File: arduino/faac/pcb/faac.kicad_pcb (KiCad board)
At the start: 2 copper layers, 5 parts, among them J1 BatCon, U1 HPD8407-F, U2 ProMini, U3 Reg3V3

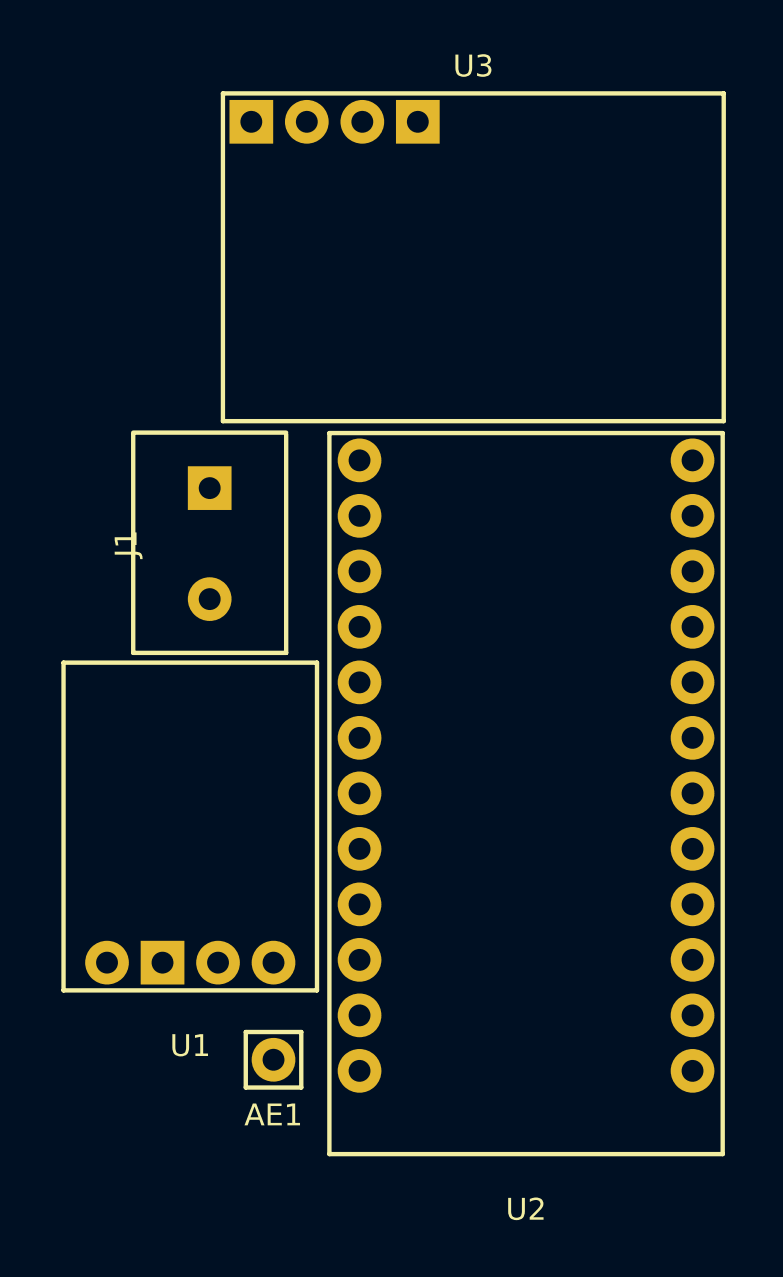
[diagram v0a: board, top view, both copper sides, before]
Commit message: faac: Add more routes
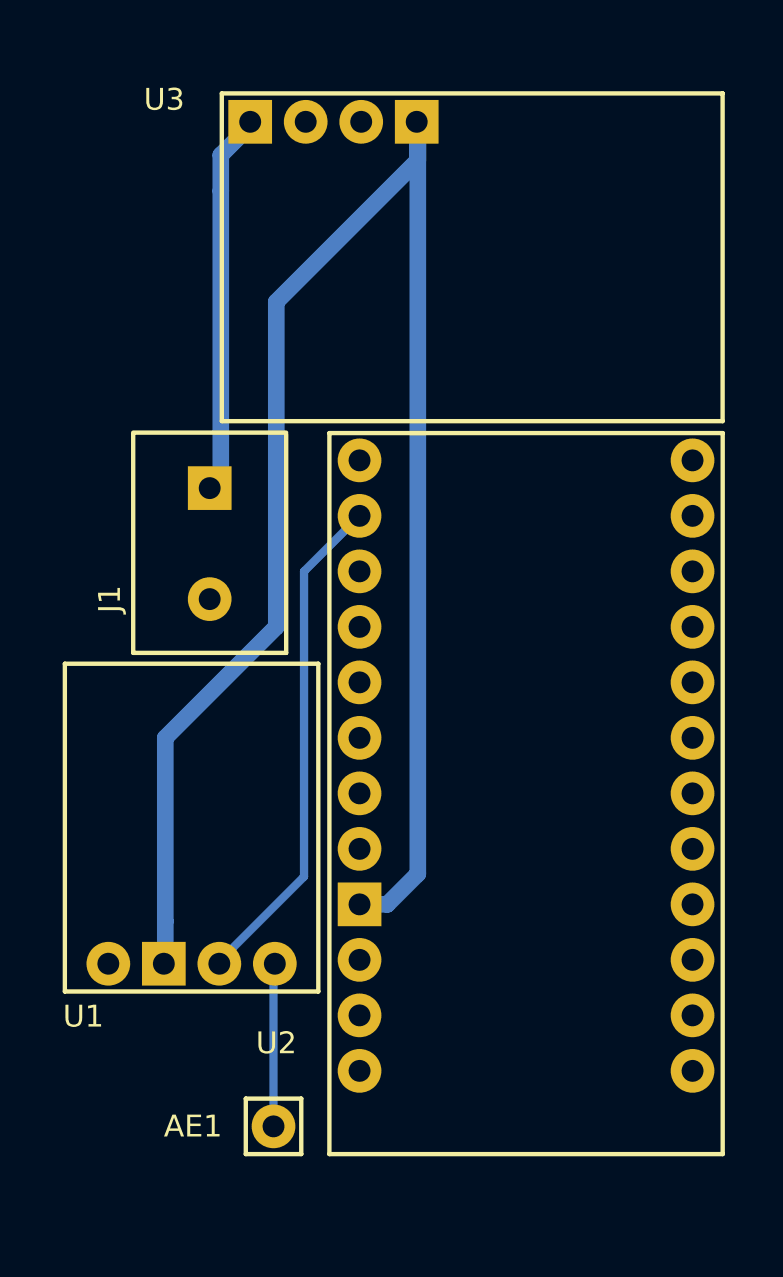
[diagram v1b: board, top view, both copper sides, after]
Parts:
- AE1: value Device_Antenna -> ANT
- moved AE1 3.05 mm to (115.4, 127.0)
- moved U1 0.08 mm to (111.7, 120.8)
- moved U3 0.05 mm to (124.5, 81.0)
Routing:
- net Net-(U1-Pad2): track 0.00 -> 80.8 mm
- net Net-(U1-Pad3): track 0.00 -> 23.0 mm
- net Net-(J1-Pad1): track 0.00 -> 17.0 mm
- net Net-(AE1-Pad1): track 0.00 -> 7.49 mm
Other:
- net class Default: clearance 0.2 -> 0.25
- rule pad_to_mask_clearance: 0.051 -> 0
- rule trace_clearance: 0.2 -> 0.25
- rule trace_min: 0.2 -> 0.25
- rule via_min_drill: 0.3 -> 0.4
- rule via_min_size: 0.4 -> 0.8
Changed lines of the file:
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@@
     (thickness 1.6)
     (drawings 0)
-    (tracks 0)
+    (tracks 16)
     (zones 0)
     (modules 5)
@@
   )
   (setup
-    (last_trace_width 0.25)
-    (trace_clearance 0.2)
+    (last_trace_width 0.381)
+    (user_trace_width 0.381)
+    (user_trace_width 0.762)
+    (trace_clearance 0.25)
     (zone_clearance 0.508)
     (zone_45_only no)
-    (trace_min 0.2)
+    (trace_min 0.25)
     (segment_width 0.2)
     (edge_width 0.15)
     (via_size 0.8)
     (via_drill 0.4)
-    (via_min_size 0.4)
-    (via_min_drill 0.3)
+    (via_min_size 0.8)
+    (via_min_drill 0.4)
     (uvia_size 0.3)
     (uvia_drill 0.1)
@@
     (pad_size 1.524 1.524)
     (pad_drill 0.762)
-    (pad_to_mask_clearance 0.051)
+    (pad_to_mask_clearance 0)
     (solder_mask_min_width 0.25)
     (aux_axis_origin 0 0)
-    (visible_elements FFFFFF7F)
+    (visible_elements 7FFFFFFF)
     (pcbplotparams
       (layerselection 0x010fc_ffffffff)
@@
   (net 25 "Net-(U2-Pad24)")
   (net_class Default "This is the default net class."
-    (clearance 0.2)
+    (clearance 0.25)
     (trace_width 0.25)
     (via_dia 0.8)
@@
     (uvia_dia 0.3)
     (uvia_drill 0.1)
+    (diff_pair_gap 0.25)
+    (diff_pair_width 0.25)
     (add_net GND)
     (add_net "Net-(AE1-Pad1)")
@@
   )
   (module myfoots:antenna (layer F.Cu)
-    (at 115.443 123.952)
-    (fp_text reference AE1 (at 0 2.54) (layer F.SilkS)
+    (at 115.443 127)
+    (fp_text reference AE1 (at -3.683 0) (layer F.SilkS)
       (effects (font (size 1 1) (thickness 0.15)))
     )
-    (fp_text value Device_Antenna (at 0 -2.54) (layer F.Fab)
+    (fp_text value ANT (at 0.127 5.08) (layer F.Fab)
       (effects (font (size 1 1) (thickness 0.15)))
     )
+    (fp_line (start -1.27 1.27) (end -1.27 -1.27) (layer F.SilkS) (width 0.2))
+    (fp_line (start 1.27 1.27) (end -1.27 1.27) (layer F.SilkS) (width 0.2))
+    (fp_line (start 1.27 -1.27) (end 1.27 1.27) (layer F.SilkS) (width 0.2))
     (fp_line (start -1.27 -1.27) (end 1.27 -1.27) (layer F.SilkS) (width 0.2))
-    (fp_line (start 1.27 -1.27) (end 1.27 1.27) (layer F.SilkS) (width 0.2))
-    (fp_line (start 1.27 1.27) (end -1.27 1.27) (layer F.SilkS) (width 0.2))
-    (fp_line (start -1.27 1.27) (end -1.27 -1.27) (layer F.SilkS) (width 0.2))
     (pad 1 thru_hole circle (at 0 0) (size 2 2) (drill 1) (layers *.Cu *.Mask)
       (net 1 "Net-(AE1-Pad1)"))
@@
   (module myfoots:BatCon (layer F.Cu)
     (at 112.522 100.33 270)
-    (fp_text reference J1 (at 0 3.81 270) (layer F.SilkS)
-      (effects (font (size 1 1) (thickness 0.2)))
-    )
-    (fp_text value BatCon (at -1.397 19.939 270) (layer F.Fab)
-      (effects (font (size 1 1) (thickness 0.2)))
-    )
+    (fp_text reference J1 (at 2.54 4.572 270) (layer F.SilkS)
+      (effects (font (size 1 1) (thickness 0.2)))
+    )
+    (fp_text value BatCon (at 0 10.922 270) (layer F.Fab)
+      (effects (font (size 1 1) (thickness 0.2)))
+    )
+    (fp_line (start -5 -3.5) (end 5 -3.5) (layer F.SilkS) (width 0.2))
+    (fp_line (start -5.08 -3.5) (end -5.08 3.5) (layer F.SilkS) (width 0.2))
+    (fp_line (start 5 -3.5) (end 5 3.5) (layer F.SilkS) (width 0.2))
     (fp_line (start -5 3.5) (end 5 3.5) (layer F.SilkS) (width 0.2))
-    (fp_line (start 5 -3.5) (end 5 3.5) (layer F.SilkS) (width 0.2))
-    (fp_line (start -5.08 -3.5) (end -5.08 3.5) (layer F.SilkS) (width 0.2))
-    (fp_line (start -5 -3.5) (end 5 -3.5) (layer F.SilkS) (width 0.2))
+    (pad 2 thru_hole circle (at 2.54 0 270) (size 2 2) (drill 1) (layers *.Cu *.Mask)
+      (net 3 GND))
     (pad 1 thru_hole rect (at -2.54 0 270) (size 2 2) (drill 1) (layers *.Cu *.Mask)
       (net 2 "Net-(J1-Pad1)"))
-    (pad 2 thru_hole circle (at 2.54 0 270) (size 2 2) (drill 1) (layers *.Cu *.Mask)
-      (net 3 GND))
   )
   (module myfoots:HPD8407-F (layer F.Cu)
-    (at 111.633 120.777)
-    (fp_text reference U1 (at 0 2.54) (layer F.SilkS)
-      (effects (font (size 1 1) (thickness 0.2)))
-    )
-    (fp_text value HPD8407-F (at 0 -16.51) (layer F.Fab)
-      (effects (font (size 1 1) (thickness 0.2)))
-    )
+    (at 111.693 120.827)
+    (fp_text reference U1 (at -4.953 1.143) (layer F.SilkS)
+      (effects (font (size 1 1) (thickness 0.2)))
+    )
+    (fp_text value HPD8407-F (at -13.843 -9.017) (layer F.Fab)
+      (effects (font (size 1 1) (thickness 0.2)))
+    )
+    (fp_line (start 5.8 -15) (end -5.8 -15) (layer F.SilkS) (width 0.2))
+    (fp_line (start -5.8 0) (end -5.8 -15) (layer F.SilkS) (width 0.2))
+    (fp_line (start 5.8 0) (end 5.8 -15) (layer F.SilkS) (width 0.2))
     (fp_line (start -5.8 0) (end 5.8 0) (layer F.SilkS) (width 0.2))
-    (fp_line (start 5.8 0) (end 5.8 -15) (layer F.SilkS) (width 0.2))
-    (fp_line (start -5.8 0) (end -5.8 -15) (layer F.SilkS) (width 0.2))
-    (fp_line (start 5.8 -15) (end -5.8 -15) (layer F.SilkS) (width 0.2))
+    (pad 1 thru_hole circle (at -3.81 -1.27) (size 2 2) (drill 1) (layers *.Cu *.Mask)
+      (net 3 GND))
+    (pad 2 thru_hole rect (at -1.27 -1.27) (size 2 2) (drill 1) (layers *.Cu *.Mask)
+      (net 5 "Net-(U1-Pad2)"))
+    (pad 4 thru_hole circle (at 3.81 -1.27) (size 2 2) (drill 1) (layers *.Cu *.Mask)
+      (net 1 "Net-(AE1-Pad1)"))
     (pad 3 thru_hole circle (at 1.27 -1.27) (size 2 2) (drill 1) (layers *.Cu *.Mask)
       (net 4 "Net-(U1-Pad3)"))
-    (pad 4 thru_hole circle (at 3.81 -1.27) (size 2 2) (drill 1) (layers *.Cu *.Mask)
-      (net 1 "Net-(AE1-Pad1)"))
-    (pad 2 thru_hole rect (at -1.27 -1.27) (size 2 2) (drill 1) (layers *.Cu *.Mask)
-      (net 5 "Net-(U1-Pad2)"))
-    (pad 1 thru_hole circle (at -3.81 -1.27) (size 2 2) (drill 1) (layers *.Cu *.Mask)
-      (net 3 GND))
   )
   (module myfoots:ProMini (layer F.Cu)
     (at 127 128.27)
-    (fp_text reference U2 (at 0 2.54) (layer F.SilkS)
-      (effects (font (size 1 1) (thickness 0.2)))
-    )
-    (fp_text value ProMini (at 0 -38.1) (layer F.Fab)
+    (fp_text reference U2 (at -11.43 -5.08) (layer F.SilkS)
+      (effects (font (size 1 1) (thickness 0.2)))
+    )
+    (fp_text value ProMini (at 13.97 -1.27) (layer F.Fab)
       (effects (font (size 1 1) (thickness 0.2)))
     )
@@
     (pad 3 thru_hole circle (at -7.62 -8.89) (size 2 2) (drill 1) (layers *.Cu *.Mask)
       (net 7 "Net-(U2-Pad3)"))
-    (pad 4 thru_hole circle (at -7.62 -11.43) (size 2 2) (drill 1) (layers *.Cu *.Mask)
+    (pad 4 thru_hole rect (at -7.62 -11.43) (size 2 2) (drill 1) (layers *.Cu *.Mask)
       (net 5 "Net-(U1-Pad2)"))
     (pad 5 thru_hole circle (at -7.62 -13.97) (size 2 2) (drill 1) (layers *.Cu *.Mask)
@@
   )
   (module myfoots:Reg3V3 (layer F.Cu)
-    (at 124.587 81.026 180)
-    (fp_text reference U3 (at 0 2.54 180) (layer F.SilkS)
-      (effects (font (size 1 1) (thickness 0.2)))
-    )
-    (fp_text value Reg3V3 (at 0 -15.24 180) (layer F.Fab)
+    (at 124.536 81.026 180)
+    (fp_text reference U3 (at 14.097 1.016 180) (layer F.SilkS)
+      (effects (font (size 1 1) (thickness 0.2)))
+    )
+    (fp_text value Reg3V3 (at -16.383 -11.684 180) (layer F.Fab)
       (effects (font (size 1 1) (thickness 0.2)))
     )
@@
       (net 5 "Net-(U1-Pad2)"))
   )
+  (segment (start 115.443 127) (end 115.443 119.507) (width 0.381) (layer B.Cu) (net 1))
+  (segment (start 113.03 84.185) (end 113.03 97.79) (width 0.762) (layer B.Cu) (net 2))
+  (segment (start 113.03 84.185) (end 113.03 82.55) (width 0.762) (layer B.Cu) (net 2))
+  (segment (start 113.03 82.55) (end 114.3 81.28) (width 0.762) (layer B.Cu) (net 2))
+  (segment (start 119.38 99.06) (end 116.84 101.6) (width 0.381) (layer B.Cu) (net 4))
+  (segment (start 116.84 101.6) (end 116.84 115.57) (width 0.381) (layer B.Cu) (net 4))
+  (segment (start 116.84 115.57) (end 113.03 119.38) (width 0.381) (layer B.Cu) (net 4))
+  (segment (start 122.047 81.026) (end 122.047 115.443) (width 0.762) (layer B.Cu) (net 5))
+  (segment (start 122.047 115.443) (end 120.65 116.84) (width 0.762) (layer B.Cu) (net 5))
+  (segment (start 120.65 116.84) (end 119.38 116.84) (width 0.762) (layer B.Cu) (net 5))
+  (segment (start 110.49 117.618) (end 110.49 109.22) (width 0.762) (layer B.Cu) (net 5))
+  (segment (start 110.49 109.22) (end 115.57 104.14) (width 0.762) (layer B.Cu) (net 5))
+  (segment (start 115.57 89.265) (end 115.57 104.14) (width 0.762) (layer B.Cu) (net 5))
+  (segment (start 122.047 82.788) (end 115.57 89.265) (width 0.762) (layer B.Cu) (net 5))
+  (segment (start 122.047 81.026) (end 122.047 82.788) (width 0.762) (layer B.Cu) (net 5))
+  (segment (start 110.49 117.618) (end 110.49 119.38) (width 0.762) (layer B.Cu) (net 5))
 )

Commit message: faac: Increase spacing
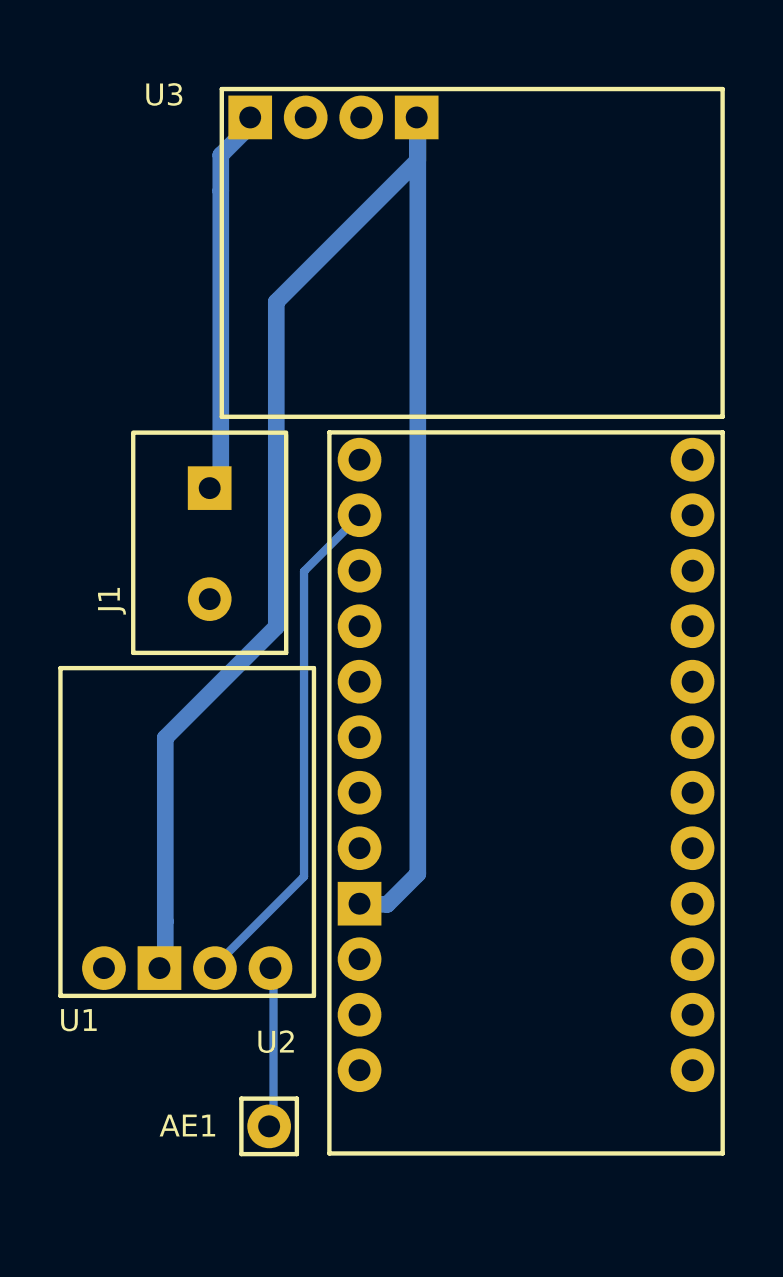
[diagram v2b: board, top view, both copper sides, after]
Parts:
- moved U1 0.28 mm to (111.5, 121.0)
- moved AE1 0.20 mm to (115.2, 127.0)
- moved U3 0.20 mm to (124.5, 80.8)
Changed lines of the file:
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@@
   )
   (setup
-    (last_trace_width 0.381)
+    (last_trace_width 0.25)
     (user_trace_width 0.381)
     (user_trace_width 0.762)
@@
   )
   (module myfoots:antenna (layer F.Cu)
-    (at 115.443 127)
+    (at 115.243 127)
     (fp_text reference AE1 (at -3.683 0) (layer F.SilkS)
       (effects (font (size 1 1) (thickness 0.15)))
@@
   )
   (module myfoots:HPD8407-F (layer F.Cu)
-    (at 111.693 120.827)
+    (at 111.493 121.027)
     (fp_text reference U1 (at -4.953 1.143) (layer F.SilkS)
       (effects (font (size 1 1) (thickness 0.2)))
@@
       (effects (font (size 1 1) (thickness 0.2)))
     )
+    (fp_line (start -5.8 0) (end 5.8 0) (layer F.SilkS) (width 0.2))
+    (fp_line (start 5.8 0) (end 5.8 -15) (layer F.SilkS) (width 0.2))
+    (fp_line (start -5.8 0) (end -5.8 -15) (layer F.SilkS) (width 0.2))
     (fp_line (start 5.8 -15) (end -5.8 -15) (layer F.SilkS) (width 0.2))
-    (fp_line (start -5.8 0) (end -5.8 -15) (layer F.SilkS) (width 0.2))
-    (fp_line (start 5.8 0) (end 5.8 -15) (layer F.SilkS) (width 0.2))
-    (fp_line (start -5.8 0) (end 5.8 0) (layer F.SilkS) (width 0.2))
-    (pad 1 thru_hole circle (at -3.81 -1.27) (size 2 2) (drill 1) (layers *.Cu *.Mask)
-      (net 3 GND))
+    (pad 3 thru_hole circle (at 1.27 -1.27) (size 2 2) (drill 1) (layers *.Cu *.Mask)
+      (net 4 "Net-(U1-Pad3)"))
+    (pad 4 thru_hole circle (at 3.81 -1.27) (size 2 2) (drill 1) (layers *.Cu *.Mask)
+      (net 1 "Net-(AE1-Pad1)"))
     (pad 2 thru_hole rect (at -1.27 -1.27) (size 2 2) (drill 1) (layers *.Cu *.Mask)
       (net 5 "Net-(U1-Pad2)"))
-    (pad 4 thru_hole circle (at 3.81 -1.27) (size 2 2) (drill 1) (layers *.Cu *.Mask)
-      (net 1 "Net-(AE1-Pad1)"))
-    (pad 3 thru_hole circle (at 1.27 -1.27) (size 2 2) (drill 1) (layers *.Cu *.Mask)
-      (net 4 "Net-(U1-Pad3)"))
+    (pad 1 thru_hole circle (at -3.81 -1.27) (size 2 2) (drill 1) (layers *.Cu *.Mask)
+      (net 3 GND))
   )
   (module myfoots:ProMini (layer F.Cu)
-    (at 127 128.27)
+    (at 127 128.24)
     (fp_text reference U2 (at -11.43 -5.08) (layer F.SilkS)
       (effects (font (size 1 1) (thickness 0.2)))
@@
   )
   (module myfoots:Reg3V3 (layer F.Cu)
-    (at 124.536 81.026 180)
+    (at 124.536 80.826 180)
     (fp_text reference U3 (at 14.097 1.016 180) (layer F.SilkS)
       (effects (font (size 1 1) (thickness 0.2)))

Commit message: faac: Add cuts
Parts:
- moved AE1 0.06 mm to (115.2, 126.9)
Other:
- board outline added: 31.7 x 50 mm
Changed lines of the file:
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@@
-(kicad_pcb (version 20171130) (host pcbnew "(5.0.2)-1")
+(kicad_pcb (version 20171130) (host pcbnew 5.0.2-bee76a0~70~ubuntu18.04.1)
   (general
     (thickness 1.6)
-    (drawings 0)
+    (drawings 4)
     (tracks 16)
     (zones 0)
@@
     (47 F.CrtYd user)
     (48 B.Fab user)
-    (49 F.Fab user)
+    (49 F.Fab user hide)
   )
   (setup
@@
   )
   (module myfoots:antenna (layer F.Cu)
-    (at 115.243 127)
+    (at 115.24 126.94)
     (fp_text reference AE1 (at -3.683 0) (layer F.SilkS)
       (effects (font (size 1 1) (thickness 0.15)))
@@
       (net 5 "Net-(U1-Pad2)"))
   )
+  (gr_line (start 105 78.9) (end 105 128.9) (layer Edge.Cuts) (width 0.15))
+  (gr_line (start 136.7 78.9) (end 105 78.9) (layer Edge.Cuts) (width 0.15))
+  (gr_line (start 136.7 128.9) (end 136.7 78.9) (layer Edge.Cuts) (width 0.15))
+  (gr_line (start 105 128.9) (end 136.7 128.9) (layer Edge.Cuts) (width 0.15))
   (segment (start 115.443 127) (end 115.443 119.507) (width 0.381) (layer B.Cu) (net 1))
   (segment (start 113.03 84.185) (end 113.03 97.79) (width 0.762) (layer B.Cu) (net 2))
